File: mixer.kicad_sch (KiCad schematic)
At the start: 74 parts, among them T1 RF_BALUN, T2 RF_BALUN, U38 BGB741L7ESD, U4 RFFC5072, U5 FM8625H, U6 FM8625H

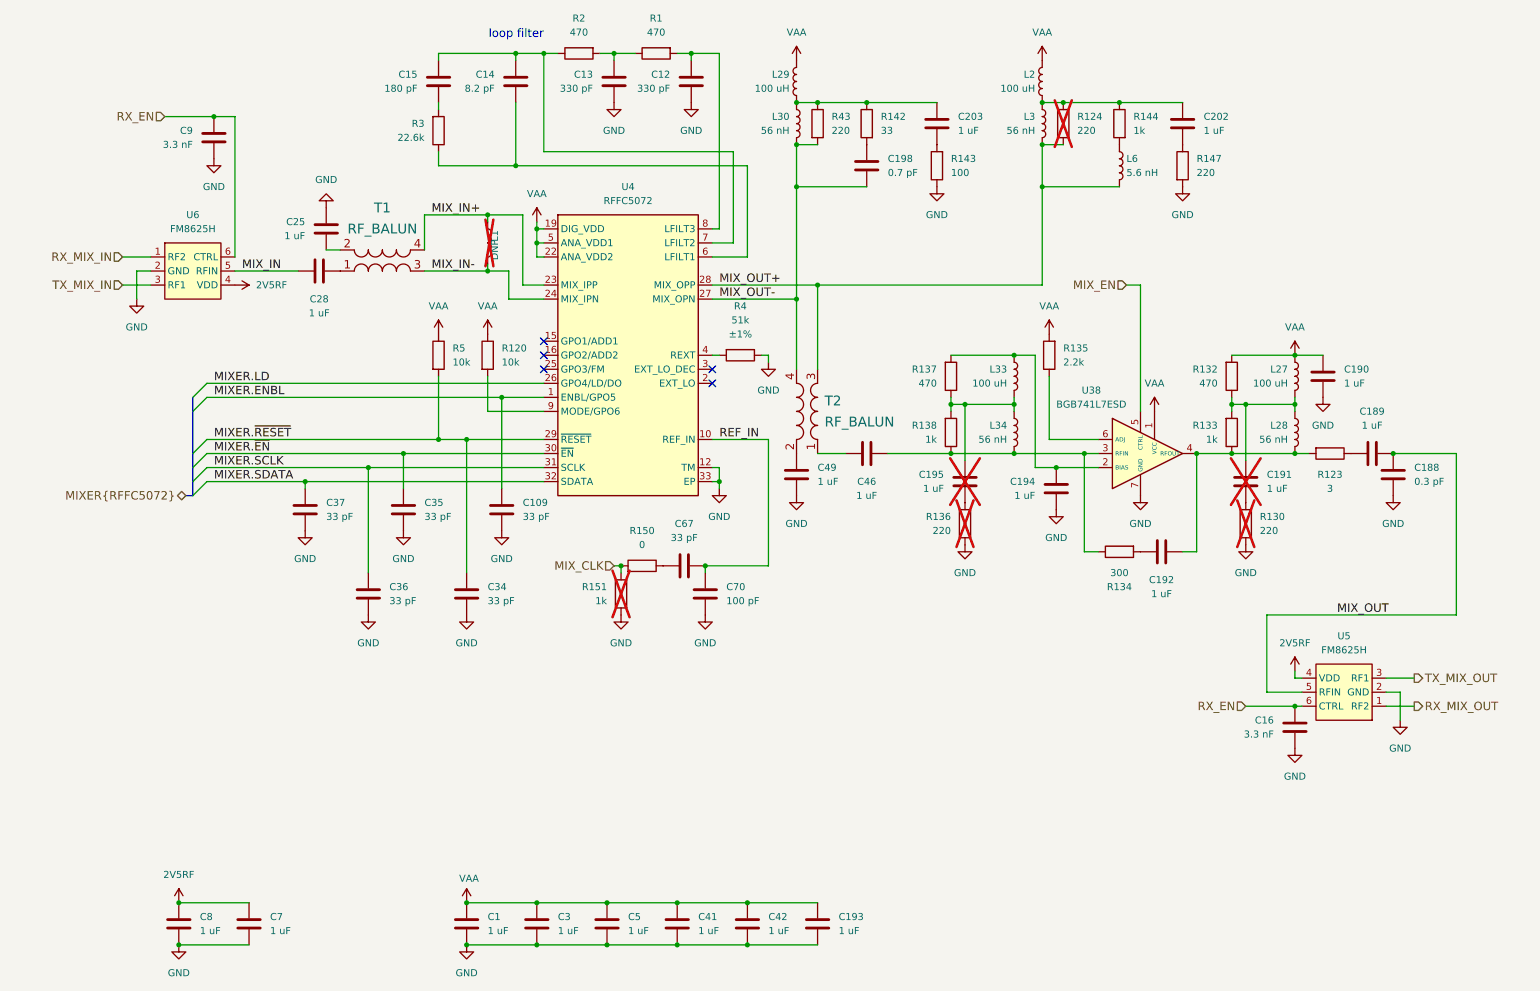
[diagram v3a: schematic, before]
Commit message: Tune mixer compensation amp
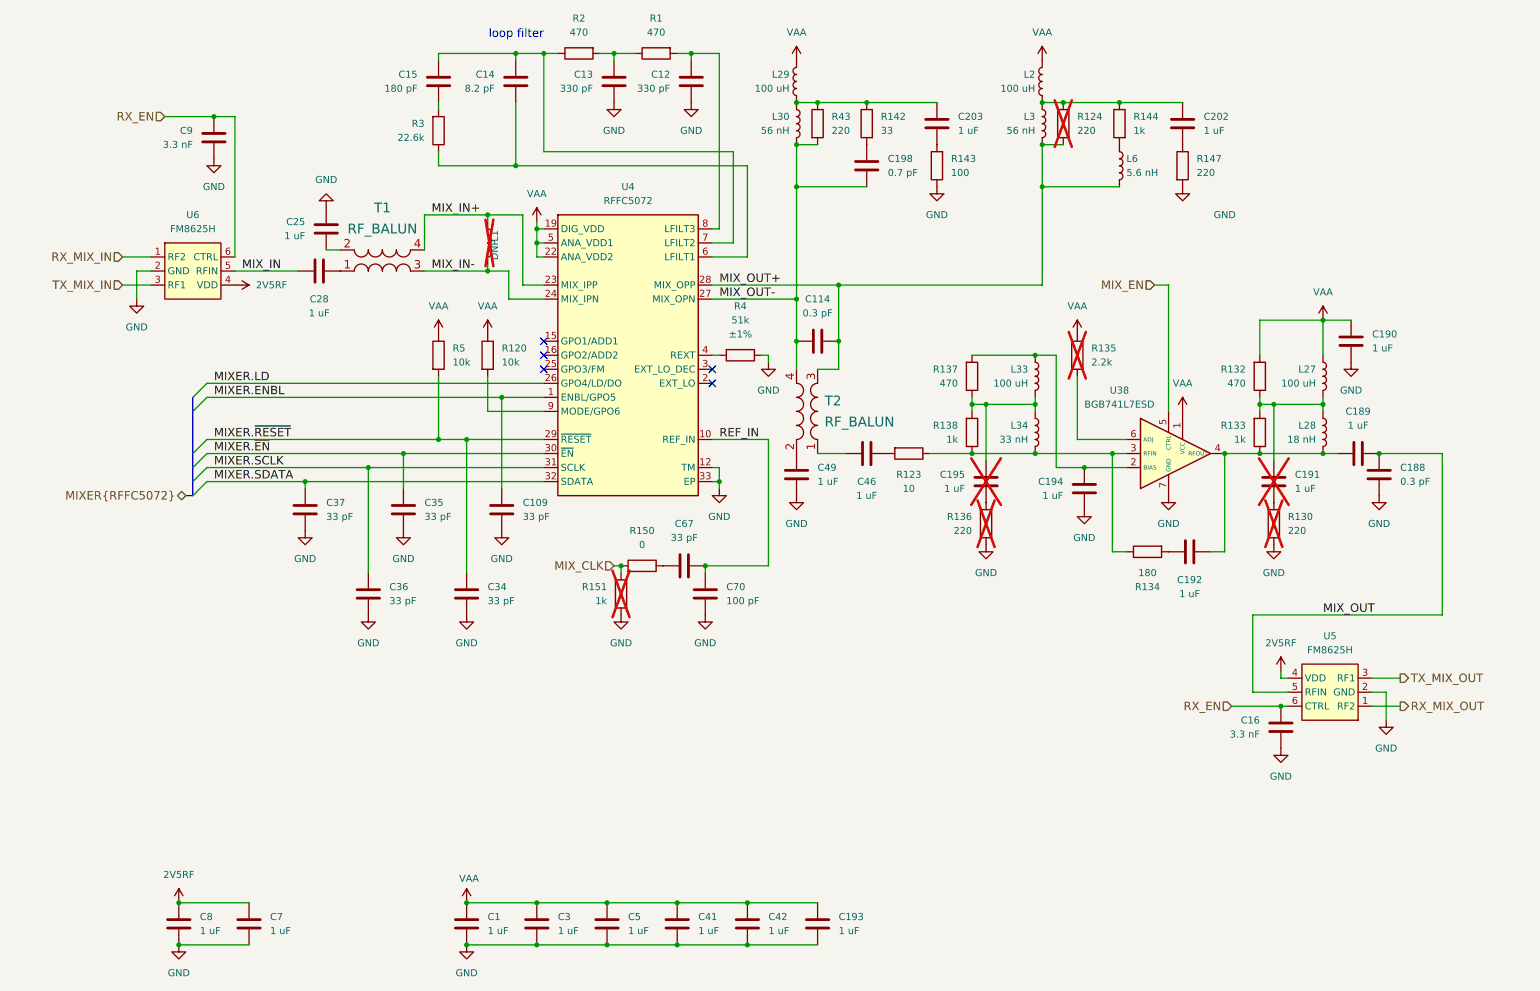
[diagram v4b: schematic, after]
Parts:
- added C114: 0.3 pF, Capacitor_SMD:C_0201_0603Metric, symbol Device:C
- L28: value 56 nH -> 18 nH; Part Number LQP03TN56NJ02D -> LQP03TN18NJ02D
- L34: value 56 nH -> 33 nH; Part Number LQP03TN56NJ02D -> LQP03TN33NJ02D
- R123: value 3 -> 10; Part Number RC0201JR-073RL -> RC0201JR-0710RL
- R134: value 300 -> 180; Part Number RC0201FR-07300RL -> RC0201JR-07180RL
- R135: now not fitted
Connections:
- net MIX_OUT+: now also C114.2
- net MIX_OUT-: now also C114.1
- net at C192.1, L28.2, R133.1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: now also C189.2; no longer R123.2
- net at R123.1: now also L34.2, R134.1, R138.1, U38.3 (RFIN); no longer C189.2
- new net: C46.1, R123.2
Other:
- moved on the sheet: C16, C188, C189, C190, C191, C192, C194, C195, L27, L28, L33, L34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

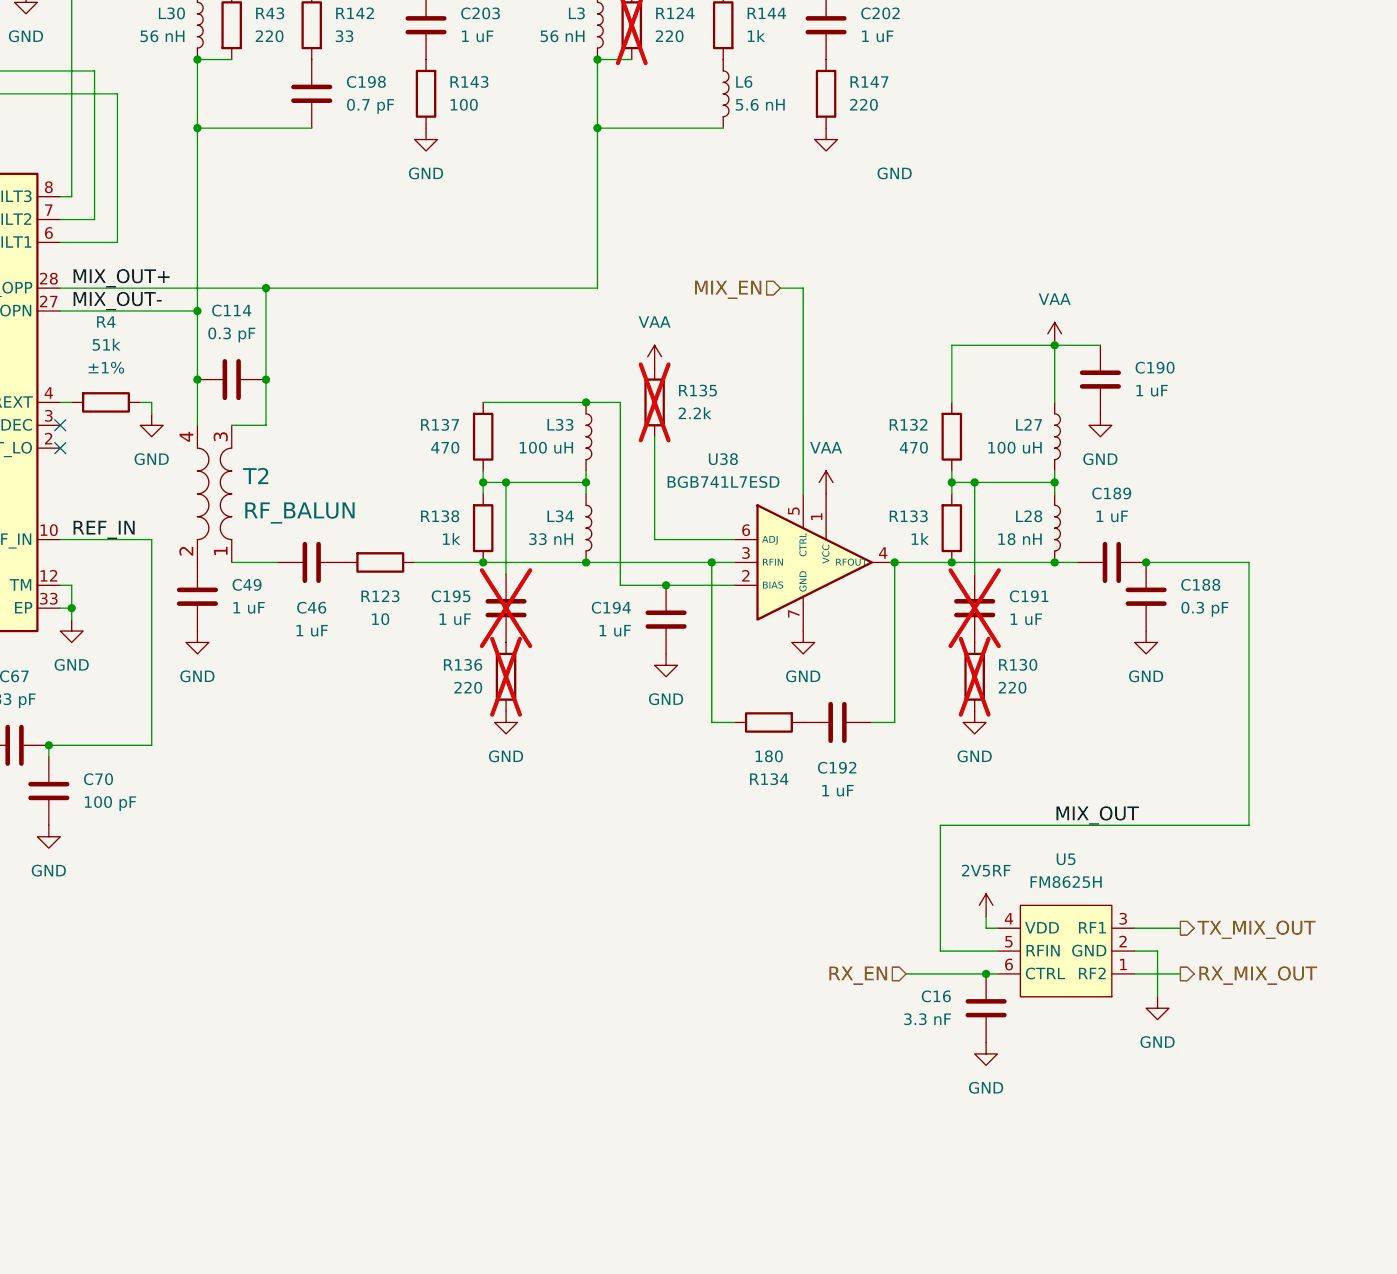
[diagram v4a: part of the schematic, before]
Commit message: Use mixer compensation amp only for TX
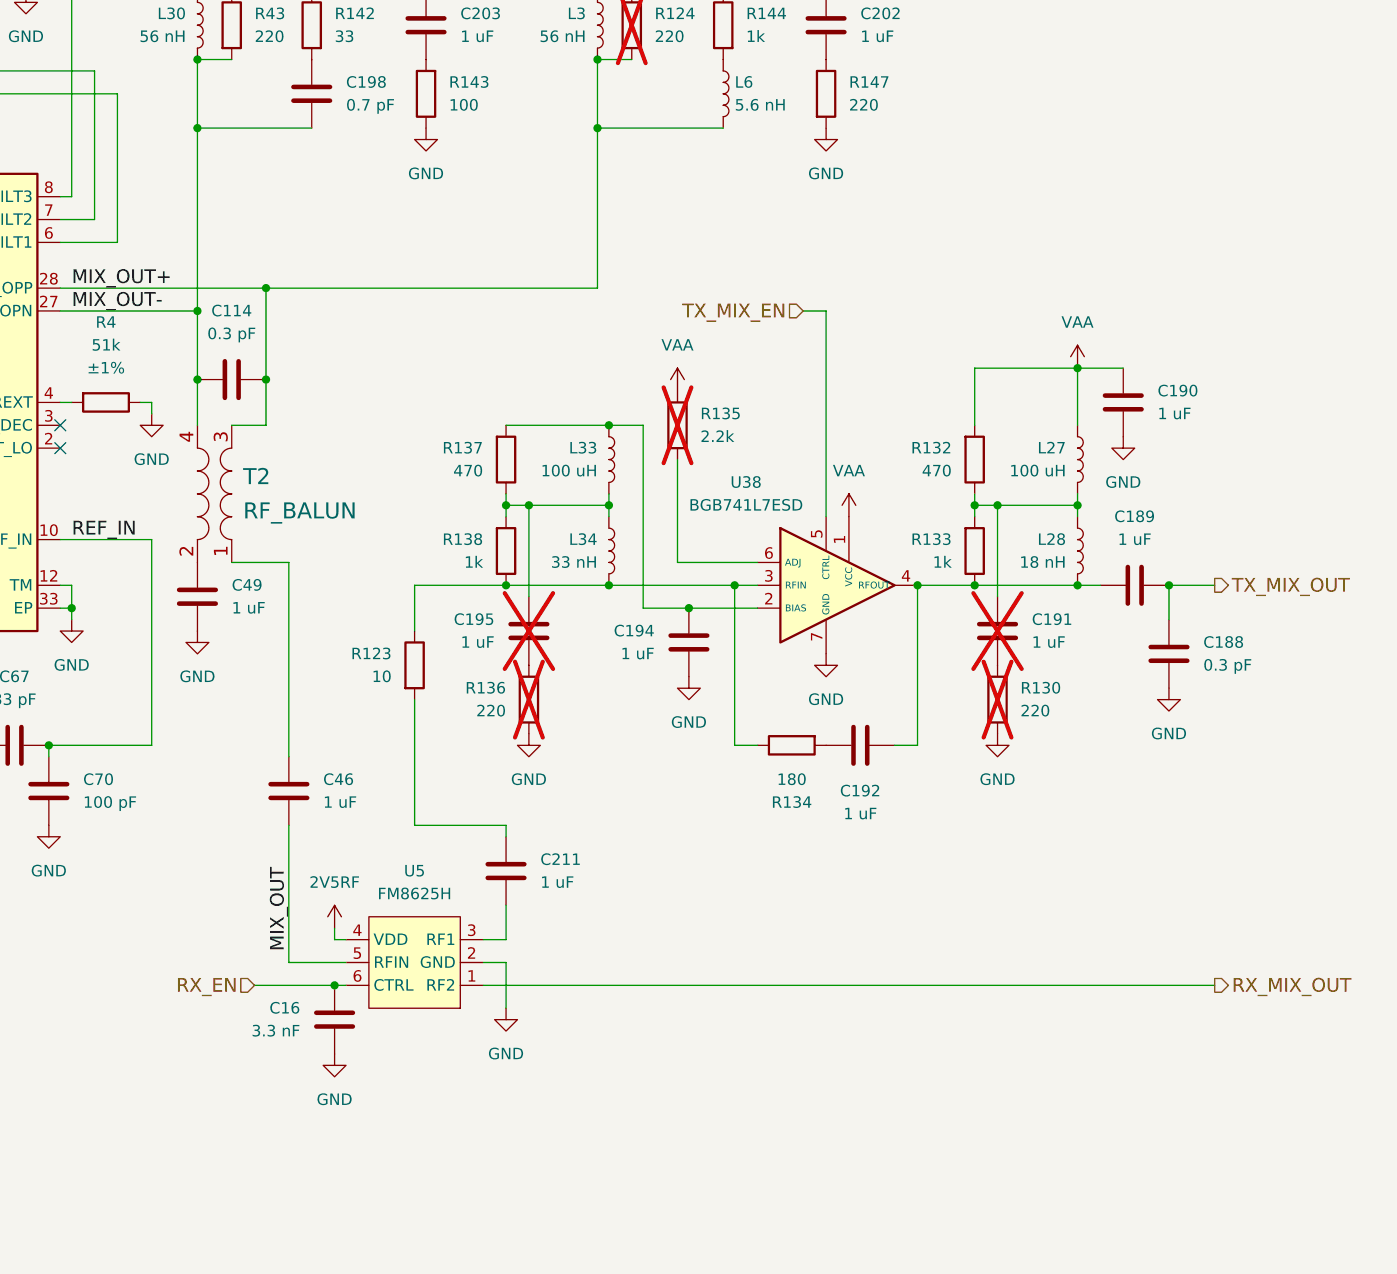
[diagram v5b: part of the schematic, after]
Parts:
- added C211: 1 uF, Capacitor_SMD:C_0201_0603Metric, symbol Device:C
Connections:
- net MIX_OUT: now also C46.1; no longer C188.1, C189.1
- net TX_MIX_OUT: now also C188.1, C189.1; no longer U5.3 (RF1)
- net at R123.2: now also C211.2; no longer C46.1
- net MIX_EN renamed TX_MIX_EN
- new net: C211.1, U5.3 (RF1)
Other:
- moved on the sheet: C16, C188, C189, C190, C191, C192, C194, C195, C46, L27, L28, L33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

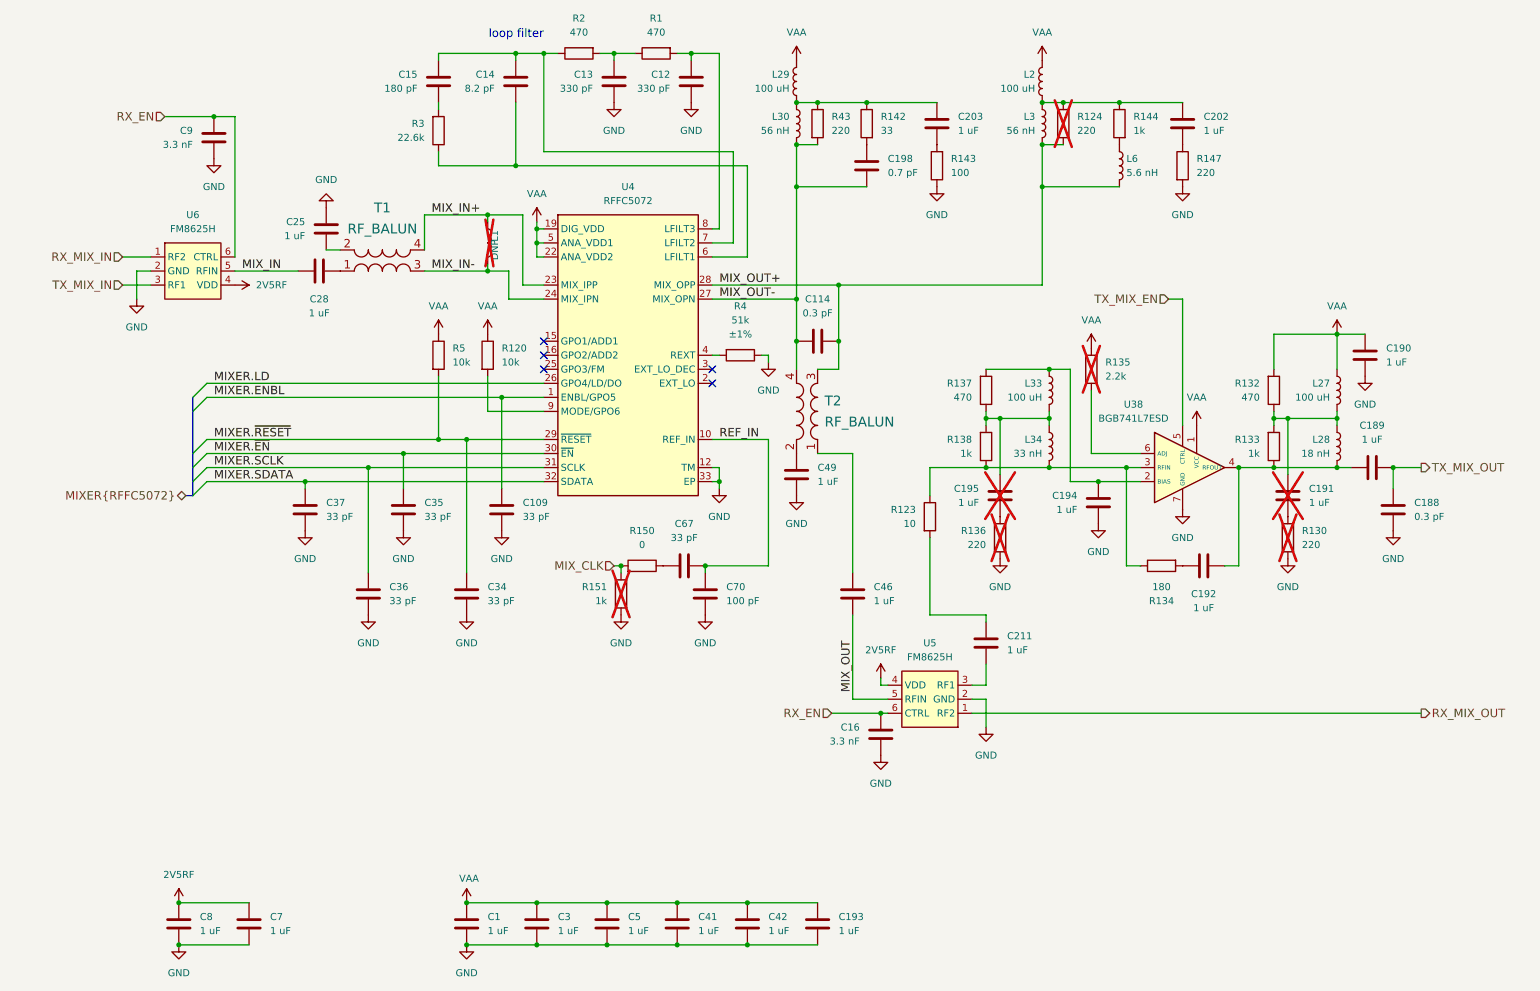
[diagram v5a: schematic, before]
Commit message: Tune mixer compensation amp
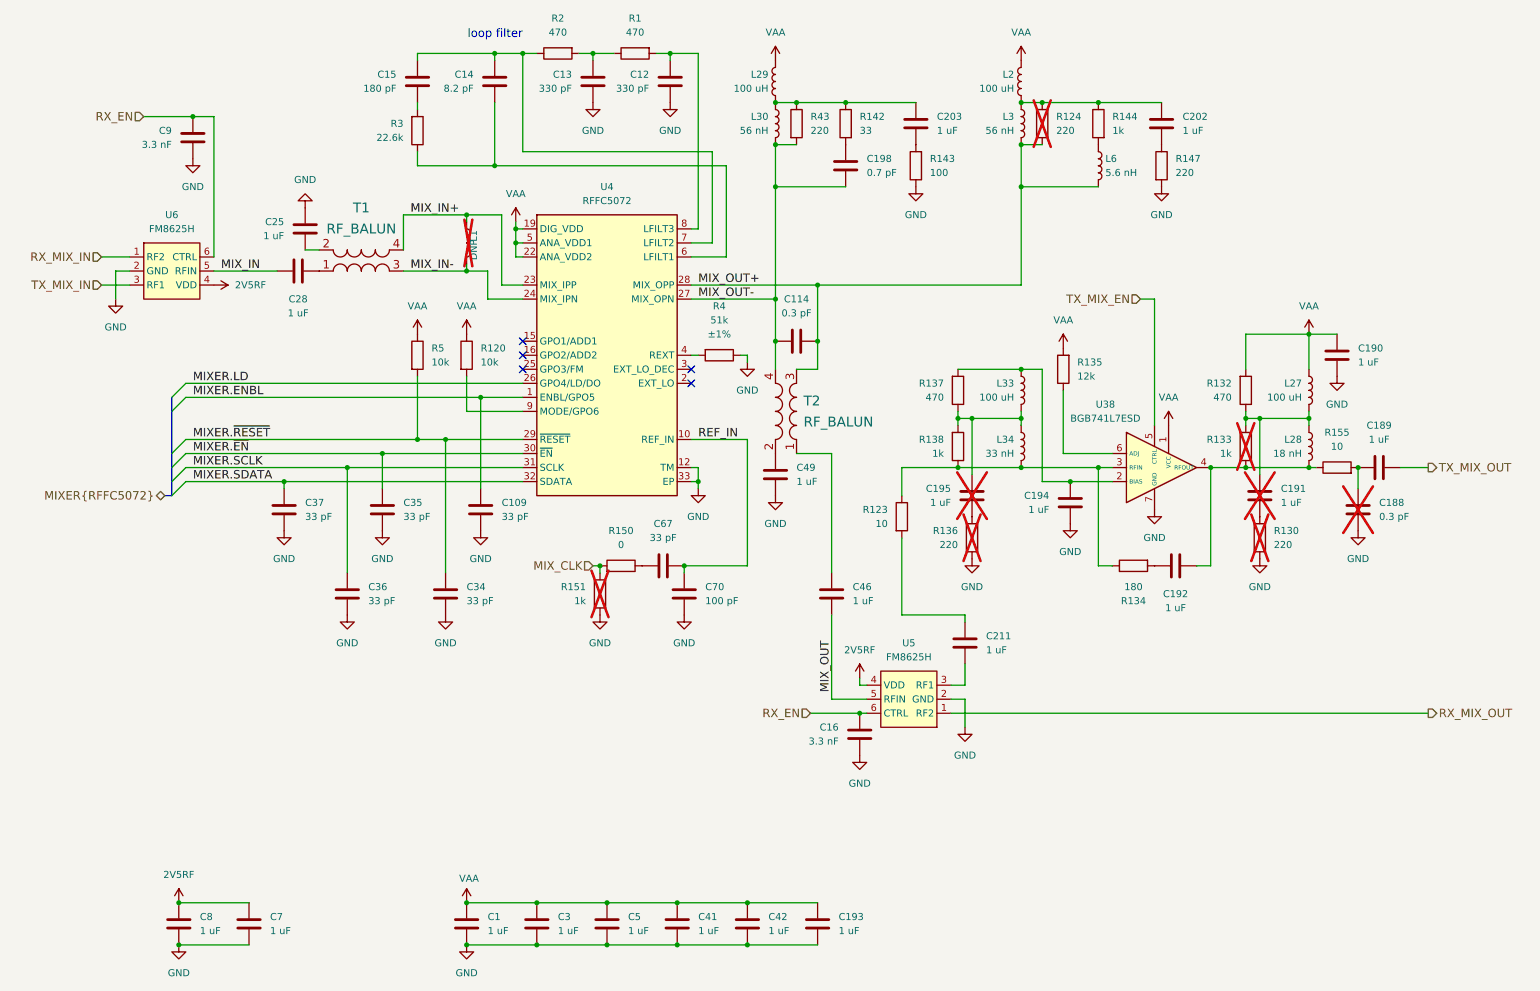
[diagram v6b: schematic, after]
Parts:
- added R155: 10, Resistor_SMD:R_0201_0603Metric, symbol Device:R
- C188, R133: now not fitted
- R135: value 2.2k -> 12k; Part Number RC0201JR-072K2L -> RC0201FR-0712KL; now fitted
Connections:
- net TX_MIX_OUT: no longer C188.1
- net at C192.1, L28.2, R133.1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: now also R155.1; no longer C189.2
- new net: C188.1, C189.2, R155.2
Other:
- moved on the sheet: C109, C114, C12, C13, C14, C15, C16, C189, C190, C191, C192, C194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
